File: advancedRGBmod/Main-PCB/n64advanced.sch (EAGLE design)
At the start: 110 parts, among them J5 2510-, J6 UPS, U1 10CL010YE144, U2 ADV7125/ADV7123, U4 74LVC3G17, U5 S25FLXXXSO8-DUAL, U6 TLV70012DDC, U7 TLV70025DDC

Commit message: remove separate eagle 7.x version
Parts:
- /COLD, /RST, B/PB, CS#, CS75#, CTRL, G/Y, HS#, P_GND0, P_GND1, P_GND2, P_GND3, P_GND4, P_VCC_3V, P_VCC_5V, R/PR, VS#: device wirepad:SMD2 -> wirepad@1:SMD2
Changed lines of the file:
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@@
 <part name="FB1" library="rcl" deviceset="R-EU_" device="R0603" value="MPZ1608S221A"/>
 <part name="GND15" library="supply1" deviceset="GND" device=""/>
-<part name="P_VCC_3V" library="wirepad" deviceset="SMD2" device=""/>
-<part name="P_GND0" library="wirepad" deviceset="SMD2" device=""/>
-<part name="D0" library="wirepad" library_urn="urn:adsk.eagle:library:412" deviceset="SMD1" device="" value=""/>
-<part name="D1" library="wirepad" library_urn="urn:adsk.eagle:library:412" deviceset="SMD1" device="" value=""/>
-<part name="D2" library="wirepad" library_urn="urn:adsk.eagle:library:412" deviceset="SMD1" device="" value=""/>
-<part name="D3" library="wirepad" library_urn="urn:adsk.eagle:library:412" deviceset="SMD1" device="" value=""/>
-<part name="D4" library="wirepad" library_urn="urn:adsk.eagle:library:412" deviceset="SMD1" device="" value=""/>
-<part name="D5" library="wirepad" library_urn="urn:adsk.eagle:library:412" deviceset="SMD1" device="" value=""/>
-<part name="D6" library="wirepad" library_urn="urn:adsk.eagle:library:412" deviceset="SMD1" device="" value=""/>
+<part name="P_VCC_3V" library="wirepad@1" deviceset="SMD2" device=""/>
+<part name="P_GND0" library="wirepad@1" deviceset="SMD2" device=""/>
+<part name="D0" library="wirepad" deviceset="SMD1" device="" value=""/>
+<part name="D1" library="wirepad" deviceset="SMD1" device="" value=""/>
+<part name="D2" library="wirepad" deviceset="SMD1" device="" value=""/>
+<part name="D3" library="wirepad" deviceset="SMD1" device="" value=""/>
+<part name="D4" library="wirepad" deviceset="SMD1" device="" value=""/>
+<part name="D5" library="wirepad" deviceset="SMD1" device="" value=""/>
+<part name="D6" library="wirepad" deviceset="SMD1" device="" value=""/>
 <part name="C1" library="rcl" deviceset="C-EU" device="C0805" value="47u"/>
 <part name="C101" library="rcl" deviceset="C-EU" device="C0805" value="10u"/>
@@
 <part name="RN11" library="resistor-net" deviceset="CTS742C083" device="" value="CAY16-47R0F4LF"/>
 <part name="RN12" library="resistor-net" deviceset="CTS742C083" device="" value="CAY16-47R0F4LF"/>
-<part name="DSYNC#" library="wirepad" library_urn="urn:adsk.eagle:library:412" deviceset="SMD1" device="" value=""/>
-<part name="CLOCK#" library="wirepad" library_urn="urn:adsk.eagle:library:412" deviceset="SMD1" device="" value=""/>
+<part name="DSYNC#" library="wirepad" deviceset="SMD1" device="" value=""/>
+<part name="CLOCK#" library="wirepad" deviceset="SMD1" device="" value=""/>
 <part name="GND11" library="supply1" deviceset="GND" device=""/>
 <part name="GND12" library="supply1" deviceset="GND" device=""/>
 <part name="U2" library="analog-devices" deviceset="ADV7123" device="" value="ADV7125/ADV7123"/>
-<part name="R/PR" library="wirepad" deviceset="SMD2" device=""/>
-<part name="G/Y" library="wirepad" deviceset="SMD2" device=""/>
-<part name="B/PB" library="wirepad" deviceset="SMD2" device=""/>
+<part name="R/PR" library="wirepad@1" deviceset="SMD2" device=""/>
+<part name="G/Y" library="wirepad@1" deviceset="SMD2" device=""/>
+<part name="B/PB" library="wirepad@1" deviceset="SMD2" device=""/>
 <part name="FB2" library="rcl" deviceset="R-EU_" device="R0603" value="MPZ1608S221A"/>
-<part name="P_VCC_5V" library="wirepad" deviceset="SMD2" device=""/>
-<part name="P_GND2" library="wirepad" deviceset="SMD2" device=""/>
+<part name="P_VCC_5V" library="wirepad@1" deviceset="SMD2" device=""/>
+<part name="P_GND2" library="wirepad@1" deviceset="SMD2" device=""/>
 <part name="C2" library="rcl" deviceset="C-EU" device="C0805" value="47u"/>
 <part name="P+1" library="supply1" deviceset="+5V" device=""/>
@@
 <part name="AGND12" library="supply1" deviceset="GND" device=""/>
 <part name="R33" library="rcl" deviceset="R-EU_" device="R0603" value="75"/>
-<part name="CS75#" library="wirepad" deviceset="SMD2" device=""/>
+<part name="CS75#" library="wirepad@1" deviceset="SMD2" device=""/>
 <part name="P+6" library="supply1" deviceset="+5V" device=""/>
 <part name="U3" library="st-microelectronics" deviceset="TSH122" device="ICT"/>
@@
 <part name="C301" library="rcl" deviceset="C-EU" device="C0805" value="10u"/>
 <part name="C302" library="rcl" deviceset="C-EU" device="C0603" value="0.01u"/>
-<part name="CS#" library="wirepad" deviceset="SMD2" device=""/>
-<part name="HS#" library="wirepad" deviceset="SMD2" device=""/>
-<part name="VS#" library="wirepad" deviceset="SMD2" device=""/>
+<part name="CS#" library="wirepad@1" deviceset="SMD2" device=""/>
+<part name="HS#" library="wirepad@1" deviceset="SMD2" device=""/>
+<part name="VS#" library="wirepad@1" deviceset="SMD2" device=""/>
 <part name="R21" library="rcl" deviceset="R-EU_" device="R0603" value="530/560"/>
 <part name="AGND9" library="supply1" deviceset="GND" device=""/>
@@
 <part name="J5" library="con-3m" deviceset="2510-" device="" value=""/>
 <part name="C109" library="rcl" deviceset="C-EU" device="C0603" value="0.1u"/>
-<part name="P_GND3" library="wirepad" deviceset="SMD2" device=""/>
-<part name="P_GND1" library="wirepad" deviceset="SMD2" device=""/>
+<part name="P_GND3" library="wirepad@1" deviceset="SMD2" device=""/>
+<part name="P_GND1" library="wirepad@1" deviceset="SMD2" device=""/>
 <part name="RN41" library="resistor-net" deviceset="CTS742C083" device="" value="CAY16-75R0F4LF"/>
 <part name="J4" library="jumper" deviceset="SJ2W" device=""/>
@@
 <part name="C501" library="rcl" deviceset="C-EU" device="C0603" value="0.1u"/>
 <part name="FB3" library="rcl" deviceset="R-EU_" device="R0603" value="MPZ1608S221A"/>
-<part name="CTRL" library="wirepad" deviceset="SMD2" device=""/>
-<part name="/RST" library="wirepad" deviceset="SMD2" device=""/>
-<part name="/COLD" library="wirepad" deviceset="SMD2" device=""/>
+<part name="CTRL" library="wirepad@1" deviceset="SMD2" device=""/>
+<part name="/RST" library="wirepad@1" deviceset="SMD2" device=""/>
+<part name="/COLD" library="wirepad@1" deviceset="SMD2" device=""/>
 <part name="GND1" library="supply1" deviceset="GND" device=""/>
 <part name="C801" library="rcl" deviceset="C-EU" device="C0603" value="0.01u"/>
@@
 <part name="AGND2" library="supply1" deviceset="GND" device=""/>
 <part name="AGND1" library="supply1" deviceset="GND" device=""/>
-<part name="U8" library="crystal-geyer_V1_0" library_urn="urn:adsk.eagle:library:203" deviceset="KXO-PXO/XO-V" device="96" package3d_urn="urn:adsk.eagle:package:11941/1"/>
+<part name="U8" library="crystal-geyer_V1_0" deviceset="KXO-PXO/XO-V" device="96"/>
 <part name="U5" library="cypress" deviceset="S25FLXXX" device="SO8-DUAL"/>
 <part name="+3V4" library="supply1" deviceset="+3V3" device=""/>
@@
 <part name="+3V11" library="supply1" deviceset="+3V3" device=""/>
 <part name="+3V12" library="supply1" deviceset="+3V3" device=""/>
-<part name="P_GND4" library="wirepad" deviceset="SMD2" device=""/>
+<part name="P_GND4" library="wirepad@1" deviceset="SMD2" device=""/>
 </parts>
 <sheets>
@@
 which will not be processed correctly with this version.
 </note>
-<note version="8.2" severity="warning">
-Since Version 8.2, EAGLE supports online libraries. The ids
-of those online libraries will not be understood (or retained)
-with this version.
-</note>
-<note version="8.3" severity="warning">
-Since Version 8.3, EAGLE supports URNs for individual library
-assets (packages, symbols, and devices). The URNs of those assets
-will not be understood (or retained) with this version.
-</note>
-<note version="8.3" severity="warning">
-Since Version 8.3, EAGLE supports the association of 3D packages
-with devices in libraries, schematics, and board files. Those 3D
-packages will not be understood (or retained) with this version.
-</note>
 </compatibility>

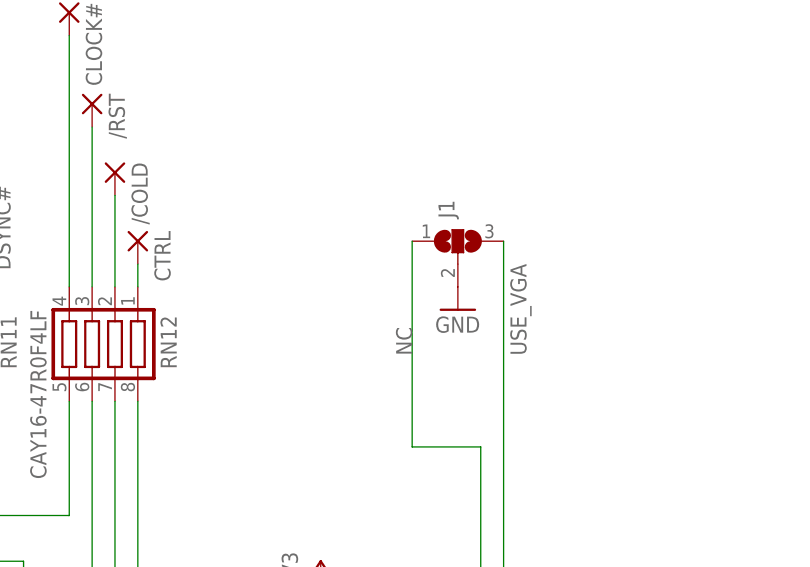
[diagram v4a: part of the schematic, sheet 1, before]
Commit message: Add filter bypass option for FilterAddOn; e.g. for simple signal conversion for PAL SNES RGB cables
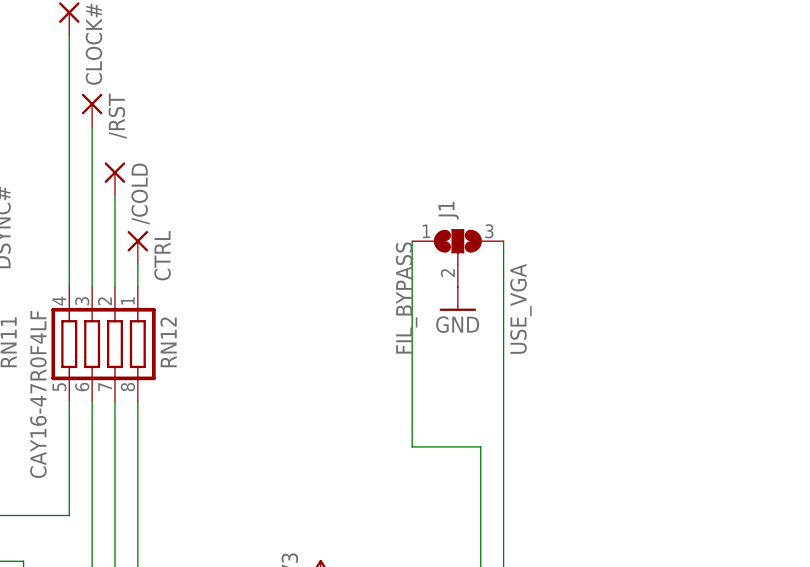
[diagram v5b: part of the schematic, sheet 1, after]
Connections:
- net NC renamed FIL_BYPASS
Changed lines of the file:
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@@
 <?xml version="1.0" encoding="utf-8"?>
 <!DOCTYPE eagle SYSTEM "eagle.dtd">
-<eagle version="8.3.2">
+<eagle version="8.4.3">
 <drawing>
 <settings>
@@
 </segment>
 </net>
-<net name="NC" class="0">
+<net name="FIL_BYPASS" class="0">
 <segment>
 <pinref part="J1" gate="G$1" pin="1"/>

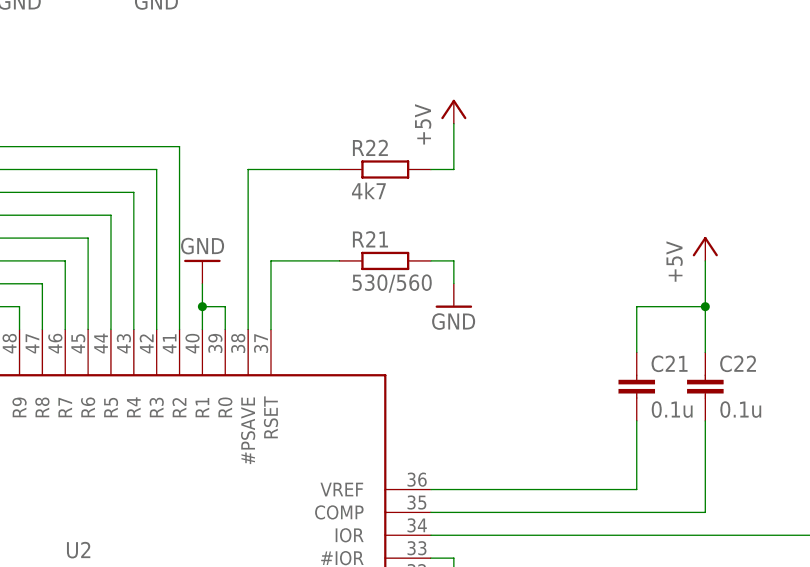
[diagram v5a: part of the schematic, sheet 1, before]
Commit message: update resistor value
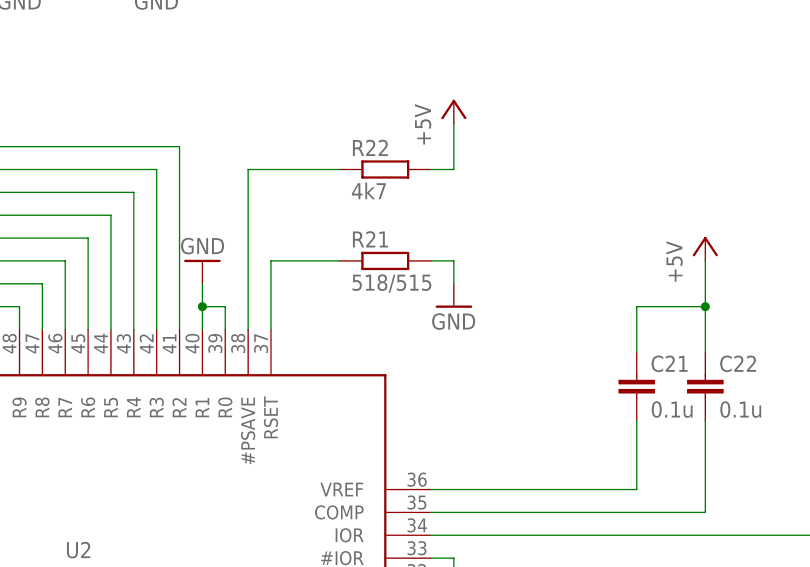
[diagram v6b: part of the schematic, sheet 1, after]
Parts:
- R21: value 530/560 -> 518/515
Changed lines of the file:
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@@
 <part name="HS#" library="wirepad@1" deviceset="SMD2" device=""/>
 <part name="VS#" library="wirepad@1" deviceset="SMD2" device=""/>
-<part name="R21" library="rcl" deviceset="R-EU_" device="R0603" value="530/560"/>
+<part name="R21" library="rcl" deviceset="R-EU_" device="R0603" value="518/515"/>
 <part name="AGND9" library="supply1" deviceset="GND" device=""/>
 <part name="R22" library="rcl" deviceset="R-EU_" device="R0603" value="4k7"/>
